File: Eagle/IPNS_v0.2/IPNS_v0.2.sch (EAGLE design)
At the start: 30 parts, among them J1 SWIM, J2 NFC, J3 BATT, J4 RIGHT CONN, J5 LEFT CONN, Q1 16MHz, Q2 32.768 kHz, U1 STM8L152C4_C6TX

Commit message: Started IPNS_v0.2
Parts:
- added C13: 100pF, IPNS_Lib_v0.1:C-USC0805
- added C14: 47pF, IPNS_Lib_v0.1:C-USC0805
- added C15: 4.7uF, IPNS_Lib_v0.1:C-USC0805
- added C16: 1u, IPNS_Lib_v0.1:C-USC0805
- added J10, J9: (no value), IPNS_Lib_v0.1:M06SILK_FEMALE_PTH
- added J6: OUTPUT CONN, IPNS_Lib_v0.1:M02PTH
- added J7: POL SWITCH CONN, IPNS_Lib_v0.1:M04PTH
- added J8: (no value), IPNS_Lib_v0.1:M02PTH
- added L1: 33uH, IPNS_Lib_v0.1:L-USL2012C
- added LED4: RED, IPNS_Lib_v0.1:LEDCHIP-LED0805
- added R10: 1k, IPNS_Lib_v0.1:R-US_M0805
- added R6: 200, IPNS_Lib_v0.1:R-US_R0805
- added R7: 2Meg, IPNS_Lib_v0.1:R-US_R0805
- added R8: 280k, IPNS_Lib_v0.1:R-US_R0805
- added R9: 1k, IPNS_Lib_v0.1:R-US_R0805
- added U$3, U$4: DMN1019USN, IPNS_Lib_v0.1:DMN1019USN
- added U$5: SLIDE_SWITCH, IPNS_Lib_v0.1:SLIDE_SWITCH
- added U2: LTC3459ES6TRMPBF, IPNS_Lib_v0.1:LTC3459ES6TRMPBF
- added U3: LT1492CS8TRPBF, IPNS_Lib_v0.1:LT1492CS8TRPBF
- R5: value 220 -> 1k
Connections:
- new net N$10: J9.6
- new net N$2: C13.1, U$3.G, U3.OUTA
- new net N$25: J9.5
- new net N$26: J9.4
- new net N$27: J9.3
- new net N$29: J10.5
- new net N$30: J10.6
- new net N$4: C13.2, R6.2, U$3.S, U3.-INA
- new net N$7: C14.1, R7.1, R8.2, U2.FB
- new net N$8: L1.1, U2.SW
- new net N$9: LED4.A, R10.2
- new net SHDN: J8.1, U2.*SHDN
- new net VBOOST: C14.2, C15.1, J7.2, R7.2, U2.VOUT, U3.V+
- new net VCASE: J6.2, J7.4
- new net VDAC: J10.3, U$4.D
- new net VELEC: J6.1, J7.3
- new net VIN: R9.2, U$4.S, U3.+INA
- new net VLOW: J7.1, U$3.D
- new net VON: C16.1, J8.2, L1.2, R10.1, U$5.OUT2, U2.VIN
- new net VPWM: J10.4, U$4.G
- net +3V3: now also J9.2
- net GND: now also C15.2, C16.2, J10.1, J9.1, LED4.C, R6.1, R8.1, R9.1, U2.GND, U3.V-
- net VBATT: now also J10.2, U$5.IN
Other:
- moved on the sheet: C1, C10, C11, C12, C2, C3, C4, C5, C6, C7, C8, C9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

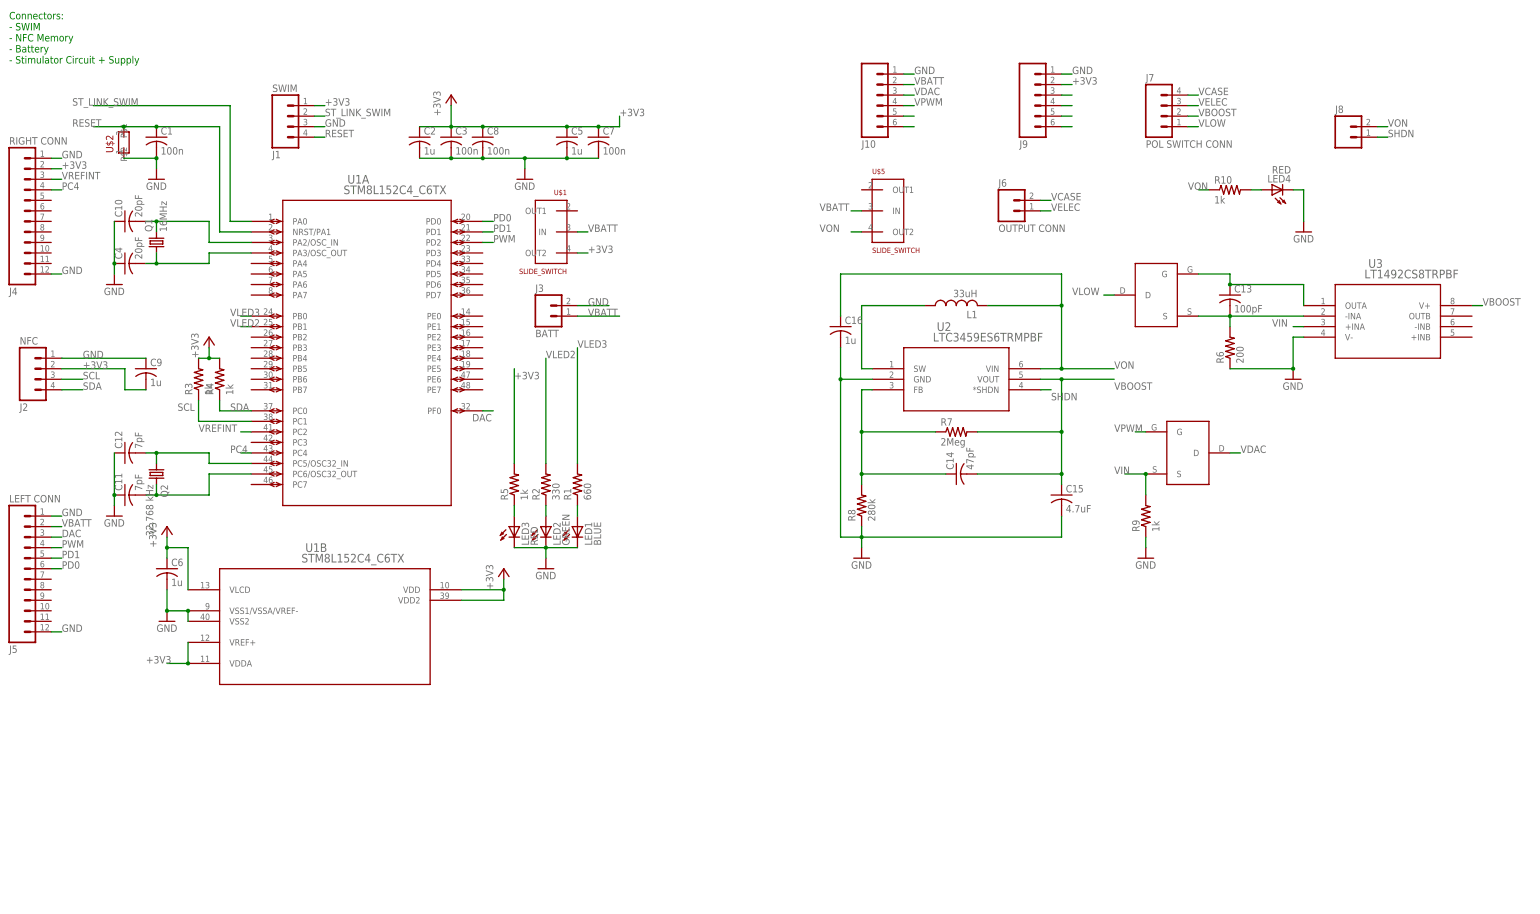
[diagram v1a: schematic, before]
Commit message: Fixed polarity switching inversion + initialization problems
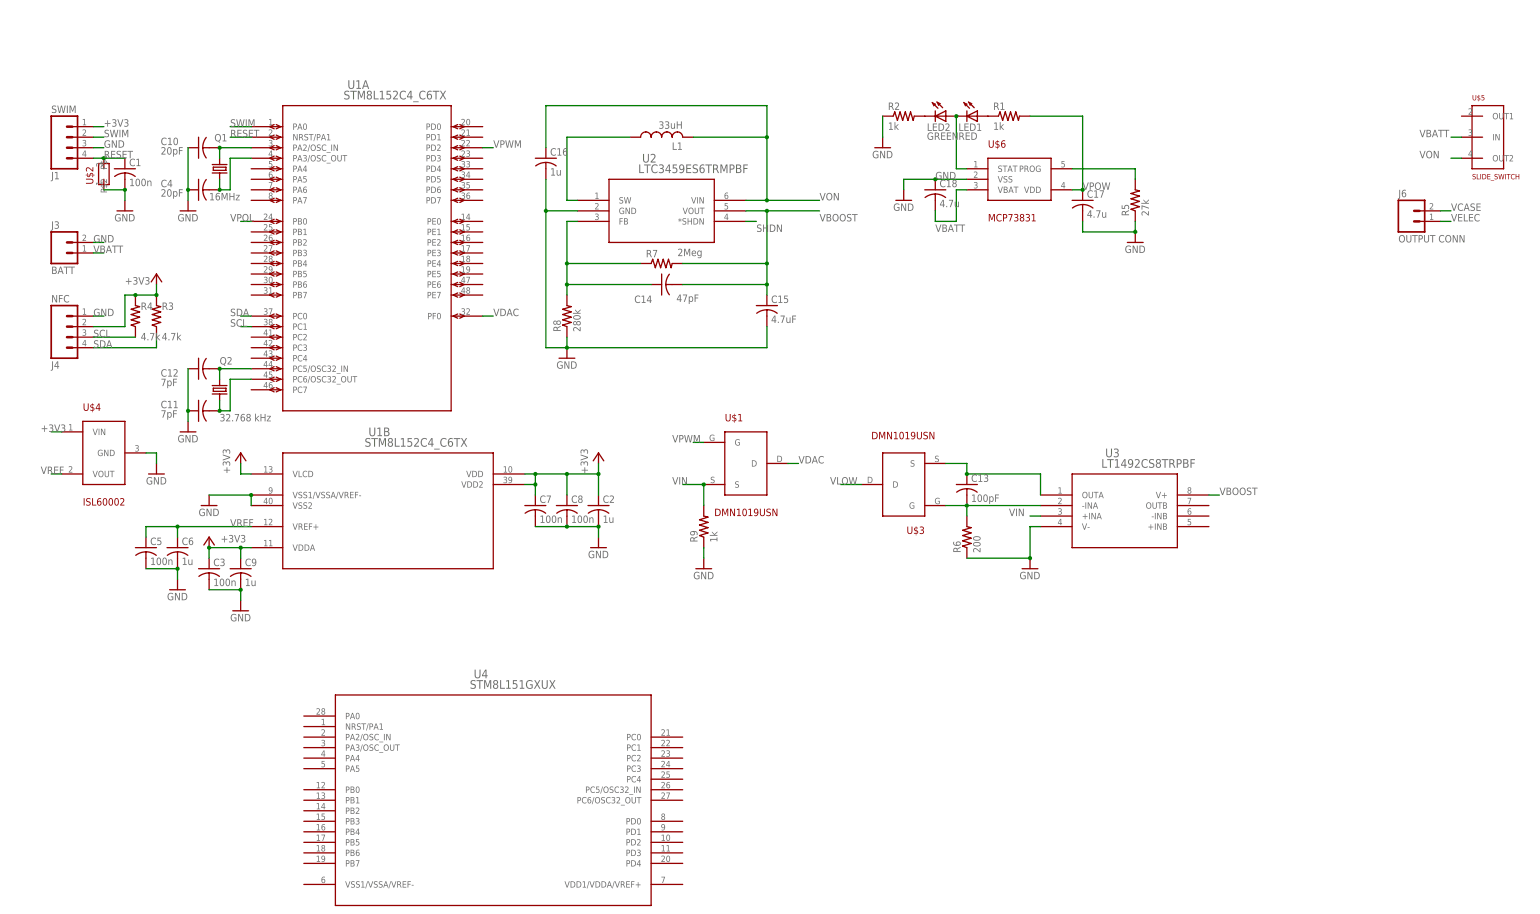
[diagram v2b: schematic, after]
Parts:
- removed J10, J9: (no value), IPNS_Lib_v0.1:M06SILK_FEMALE_PTH
- removed J2: NFC, IPNS_Lib_v0.1:M04PTH
- removed J5: LEFT CONN, IPNS_Lib_v0.1:M12PTH
- removed J7: POL SWITCH CONN, IPNS_Lib_v0.1:M04PTH
- removed J8: (no value), IPNS_Lib_v0.1:M02PTH
- removed LED3: RED, led:LEDCHIP-LED0805
- removed LED4: RED, IPNS_Lib_v0.1:LEDCHIP-LED0805
- removed R10: 1k, IPNS_Lib_v0.1:R-US_M0805
- added C17, C18: 4.7u, IPNS_Lib:C-USC0603
- added U$6: MCP78381, IPNS_Lib:MCP78381
- added U4: STM8L151GXUX, IPNS_Lib:STM8L151GXUX
- C1, C10, C11, C12, C13, C14, C15, C16, C2, C3, C4, C6, C7, C8, C9: device IPNS_Lib_v0.1:C-USC0805 -> IPNS_Lib_v0.1:C-USC0603
- C5: value 1u -> 100n; device IPNS_Lib_v0.1:C-USC0805 -> IPNS_Lib_v0.1:C-USC0603
- J4: value RIGHT CONN -> NFC; device IPNS_Lib_v0.1:M12PTH -> IPNS_Lib_v0.1:M04PTH
- L1: device IPNS_Lib_v0.1:L-USL2012C -> IPNS_Lib_v0.1:L-USL0201
- LED1: value BLUE -> RED; device led:LEDCHIP-LED0805 -> IPNS_Lib:LEDSML0603
- LED2: device led:LEDCHIP-LED0805 -> IPNS_Lib:LEDSML0603
- R1: value 660 -> 1k; device IPNS_Lib_v0.1:R-US_R0805 -> IPNS_Lib:R-US_R0603
- R2: value 330 -> 1k; device IPNS_Lib_v0.1:R-US_R0805 -> IPNS_Lib:R-US_R0603
- R3, R4: value 1k -> 4.7k; device IPNS_Lib_v0.1:R-US_R0805 -> IPNS_Lib_v0.1:R-US_R0603
- R5: value 1k -> 27k; device IPNS_Lib_v0.1:R-US_R0805 -> IPNS_Lib:R-US_R0603
- R6, R7, R8, R9: device IPNS_Lib_v0.1:R-US_R0805 -> IPNS_Lib_v0.1:R-US_R0603
- U$1: value SLIDE_SWITCH -> DMN1019USN; device IPNS_Lib_v0.1:SLIDE_SWITCH -> IPNS_Lib:DMN1019USN
- U$3: device IPNS_Lib_v0.1:DMN1019USN -> IPNS_Lib:DMN1019USN
- U$4: value DMN1019USN -> ISL60002; device IPNS_Lib_v0.1:DMN1019USN -> IPNS_Lib:ISL60002
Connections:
- net ST_LINK_SWIM renamed SWIM
- removed net DAC: J5.3, U1A.PF0
- removed net N$11 (its old number): LED3.A, R5.1
- removed net N$12: LED2.A, R2.1
- removed net N$25: J9.5
- removed net N$26: J9.4
- removed net N$27: J9.3
- removed net N$29: J10.5
- removed net N$30: J10.6
- removed net N$9 (its old number): LED4.A, R10.2
- removed net PC4: J4.4, U1A.PC4
- removed net PD0: J5.6, U1A.PD0
- removed net PD1: J5.5, U1A.PD1
- removed net PWM: J5.4, U1A.PD2
- removed net VLED2: R2.2, U1A.PB1
- removed net VLED3: R1.2, U1A.PB0
- removed net VREFINT: J4.3, U1A.PC2
- new net N$1: LED1.C, LED2.A, U$6.STAT
- new net N$13: R5.2, U$6.PROG
- new net VPOL: U1A.PB0
- new net VPOW: C17.1, R1.2, U$6.VDD
- new net VREF: C5.1, C6.1, U$4.VOUT, U1B.VREF+
- net +3V3: now also C9.1, U$4.VIN; no longer C5.1, C6.1, C9.2, J2.2, J9.2, R5.2, U$1.OUT2, U1B.VREF+
- net GND: now also C17.2, C18.1, C9.2, R2.1, R5.1, U$4.GND, U$6.VSS; no longer C9.1, J10.1, J2.1, J4.12, J5.1, J5.12, J9.1, LED1.C, LED2.C, LED3.C, LED4.C
- net N$10: now also LED2.C, R2.2; no longer J9.6
- net N$2: now also U$3.S; no longer U$3.G
- net N$4: now also U$3.G; no longer U$3.S
- net SCL: now also J4.3, R4.1; no longer J2.3, R3.1
- net SDA: now also J4.4, R3.1; no longer J2.4, R4.1
- net SHDN: no longer J8.1
- net VBATT: now also C18.2, U$6.VBAT; no longer J10.2, J5.2, U$1.IN
- net VBOOST: no longer J7.2
- net VCASE: no longer J7.4
- net VDAC: now also U$1.D, U1A.PF0; no longer J10.3, U$4.D
- net VELEC: no longer J7.3
- net VIN: now also U$1.S; no longer U$4.S
- net VLOW: no longer J7.1
- net VON: no longer J8.2, R10.1
- net VPWM: now also U$1.G, U1A.PD2; no longer J10.4, U$4.G
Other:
- note removed: "Connectors: - SWIM - NFC Memory - Battery - Stimulator Circuit + Supply"
- moved on the sheet: C1, C10, C11, C12, C13, C14, C15, C16, C2, C3, C4, C5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

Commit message: Developed IPNS_v0.2 further
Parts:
- removed J6: OUTPUT CONN, IPNS_Lib_v0.1:M02PTH
- removed Q1: 16MHz, IPNS_Lib_v0.1:CRYSTALHC49S
- removed Q2: 32.768 kHz, IPNS_Lib_v0.1:CRYSTALTC26H
- removed U4: STM8L151GXUX, IPNS_Lib:STM8L151GXUX
- added C19: 10u, IPNS_Lib:C-USC0603
- added C20, C22: 0.1u, rcl:C-USC0603
- added C21: 22u, rcl:C-USC0603
- added IC1: TPS61201, IPNS_Lib:TPS61200
- added J2: (no value), IPNS_Lib:M02PTH
- added L2: 2.2u, rcl:L-USL2012C
- added R10: 1k, IPNS_Lib:R-US_R0603
- added R11: 220k, rcl:R-US_R0603
- added R12: 1.2Meg, rcl:R-US_R0603
- added R13: 2Meg, rcl:R-US_R0603
- added R14: 180k, rcl:R-US_R0603
- added U$7: 40_CRYSTAL_16M, IPNS_Lib:40_CRYSTAL_16M
- added U$8: 32.768_CRYSTAL, IPNS_Lib:32.768_CRYSTAL
- L1: device IPNS_Lib_v0.1:L-USL0201 -> IPNS_Lib_v0.1:L-USL2012C
- U$5: value SLIDE_SWITCH -> ADG1636; device IPNS_Lib_v0.1:SLIDE_SWITCH -> IPNS_Lib:ADG1636
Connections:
- net VPWM renamed VTIM
- removed net N$5: C4.2, Q1.1, U1A.PA3/OSC_OUT
- removed net N$9: C10.2, Q1.2, U1A.PA2/OSC_IN
- removed net VCASE: J6.2
- removed net VLOW: U$3.D
- removed net VON: C16.1, L1.2, U$5.OUT2, U2.VIN
- new net N$12: C13.2, U$3.G, U3.OUTA
- new net N$14: IC1.L, L2.2
- new net N$16: IC1.FB, R11.2, R12.1
- new net N$17: C20.1, IC1.VAUX
- new net N$18: C22.2, IC1.UVLO, R13.1, R14.2
- new net N$22: U$5.2S1A, U$5.EN14, U$5.S2B12, U$5.VDD13
- new net OSC161: C4.1, U$7.3, U1A.PA2/OSC_IN
- new net OSC162: C10.2, U$7.1, U1A.PA3/OSC_OUT
- new net VBODY: U$5.3D1
- new net VSINK: U$3.D, U$5.4S1B, U$5.S2A10
- net +3V3: now also C21.1, IC1.VOUT, R10.2, R12.2
- net GND: now also C19.2, C20.2, C21.2, C4.2, IC1.GND, IC1.PGND, IC1.PP, IC1.PP@1, IC1.PP@2, J2.2, R11.1, R14.1, U$5.5VSS, U$5.6GND, U$7.2, U$7.4, U3.+INB; no longer C4.1
- net N$2: now also R6.2, U3.-INA; no longer U3.OUTA
- net N$3: now also U$8.1; no longer Q2.2
- net N$4: now also U3.-INB, U3.OUTB; no longer C13.2, R6.2, U$3.G, U3.-INA
- net N$6: now also U$8.2; no longer Q2.1
- net RESET: now also R10.1
- net VBATT: now also C16.1, C19.1, C22.1, IC1.EN, IC1.PS, IC1.VIN, L1.2, L2.1, R13.2, U2.VIN; no longer U$5.IN
- net VELEC: now also U$5.D211; no longer J6.1
- net VPOL: now also U$5.1IN1, U$5.IN29
- net VPOW: now also J2.1
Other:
- moved on the sheet: C1, C10, C13, C14, C15, C16, C17, C18, C2, C3, C4, C5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

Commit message: Updated IPNS_v0.2
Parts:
- removed C5, C7, C8: 100n, IPNS_Lib_v0.1:C-USC0603
- removed C6, C9: 1u, IPNS_Lib_v0.1:C-USC0603
- removed J2: (no value), IPNS_Lib:M02PTH
- removed J3: BATT, IPNS_Lib_v0.1:M02PTH
- removed R10: 1k, IPNS_Lib:R-US_R0603
- removed R11: 220k, rcl:R-US_R0603
- removed R12: 1.2Meg, rcl:R-US_R0603
- removed U1: STM8L152C4_C6TX, IPNS_Lib_v0.1:STM8L152C4_C6TX
- added J5, J6: (no value), IPNS_Lib:M12PTH
- added U$10, U$9: SCREWTERMINAL, IPNS_Lib:SCREWTERMINAL
- added U4: STM8L151GXUX, IPNS_Lib:STM8L151GXUX
- U$4: value ISL60002 -> SCREWTERMINAL; device IPNS_Lib:ISL60002 -> IPNS_Lib:SCREWTERMINAL
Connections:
- removed net N$16: IC1.FB, R11.2, R12.1
- removed net N$3: C11.2, U$8.1, U1A.PC6/OSC32_OUT
- removed net N$6: C12.2, U$8.2, U1A.PC5/OSC32_IN
- removed net OSC161: C4.1, U$7.3, U1A.PA2/OSC_IN
- removed net OSC162: C10.2, U$7.1, U1A.PA3/OSC_OUT
- removed net SHDN: U2.*SHDN
- removed net VREF: C5.1, C6.1, U$4.VOUT, U1B.VREF+
- new net OSCH1: C4.1, U$7.3, U4.PA3/OSC_OUT
- new net OSCH2: C10.2, U$7.1, U4.PA2/OSC_IN
- new net OSCL1: C12.2, U$8.2, U4.PC5/OSC32_IN
- new net OSCL2: C11.2, U$8.1, U4.PC6/OSC32_OUT
- net +3V3: now also IC1.FB, U4.VDD1/VDDA/VREF+; no longer C7.1, C8.1, C9.1, R10.2, R12.2, U$4.VIN, U1B.VDD, U1B.VDD2, U1B.VDDA, U1B.VLCD
- net GND: now also U$10.2, U$4.2, U4.VSS1/VSSA/VREF-; no longer C5.2, C6.2, C7.2, C8.2, C9.2, J2.2, J3.2, R11.1, U$4.GND, U1B.VSS1/VSSA/VREF-, U1B.VSS2
- net RESET: now also U4.NRST/PA1; no longer R10.1, U1A.NRST/PA1
- net SCL: now also U4.PC1; no longer U1A.PC1
- net SDA: now also U4.PC0; no longer U1A.PC0
- net SWIM: now also U4.PA0; no longer U1A.PA0
- net VBATT: now also U$10.1, U2.*SHDN; no longer J3.1
- net VBODY: now also U$9.1
- net VDAC: now also U4.PB5; no longer U1A.PF0
- net VELEC: now also U$9.2
- net VPOL: now also U4.PB0; no longer U1A.PB0
- net VPOW: now also U$4.1; no longer J2.1
- net VTIM: now also U4.PD2; no longer U1A.PD2
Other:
- moved on the sheet: C1, C10, C11, C12, C13, C14, C15, C16, C17, C18, C19, C2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
